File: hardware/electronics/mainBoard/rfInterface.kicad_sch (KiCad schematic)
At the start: 21 parts, among them J12 CONMHF1-SMD-T, J13 CONMHF1-SMD-T, J14 CONMHF1-SMD-T, J15 CONMHF1-SMD-T, U16 PMA2-162LNA+, U17 QCN-19D+

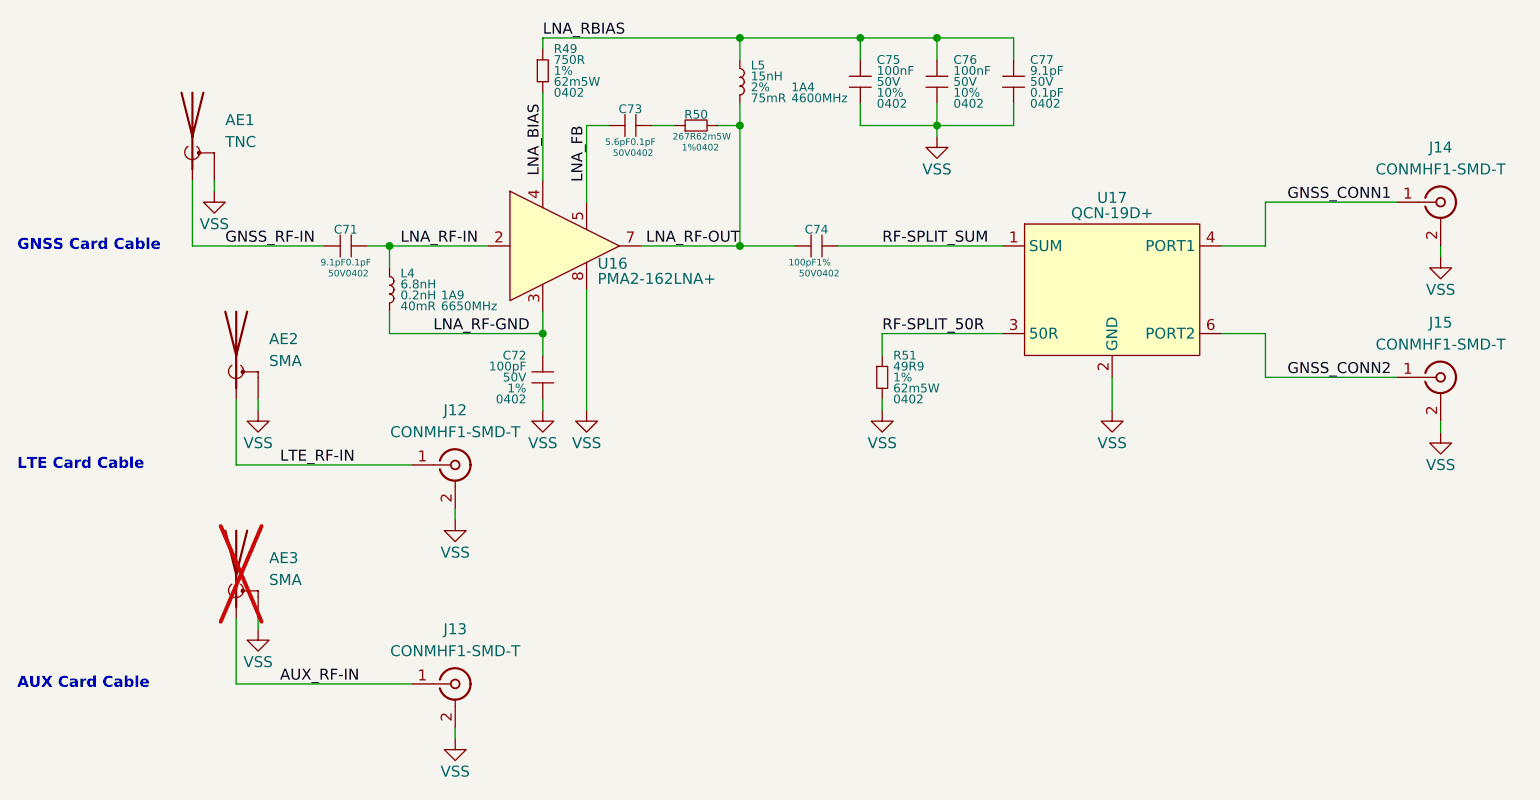
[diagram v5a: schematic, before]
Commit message: updated symbol refs
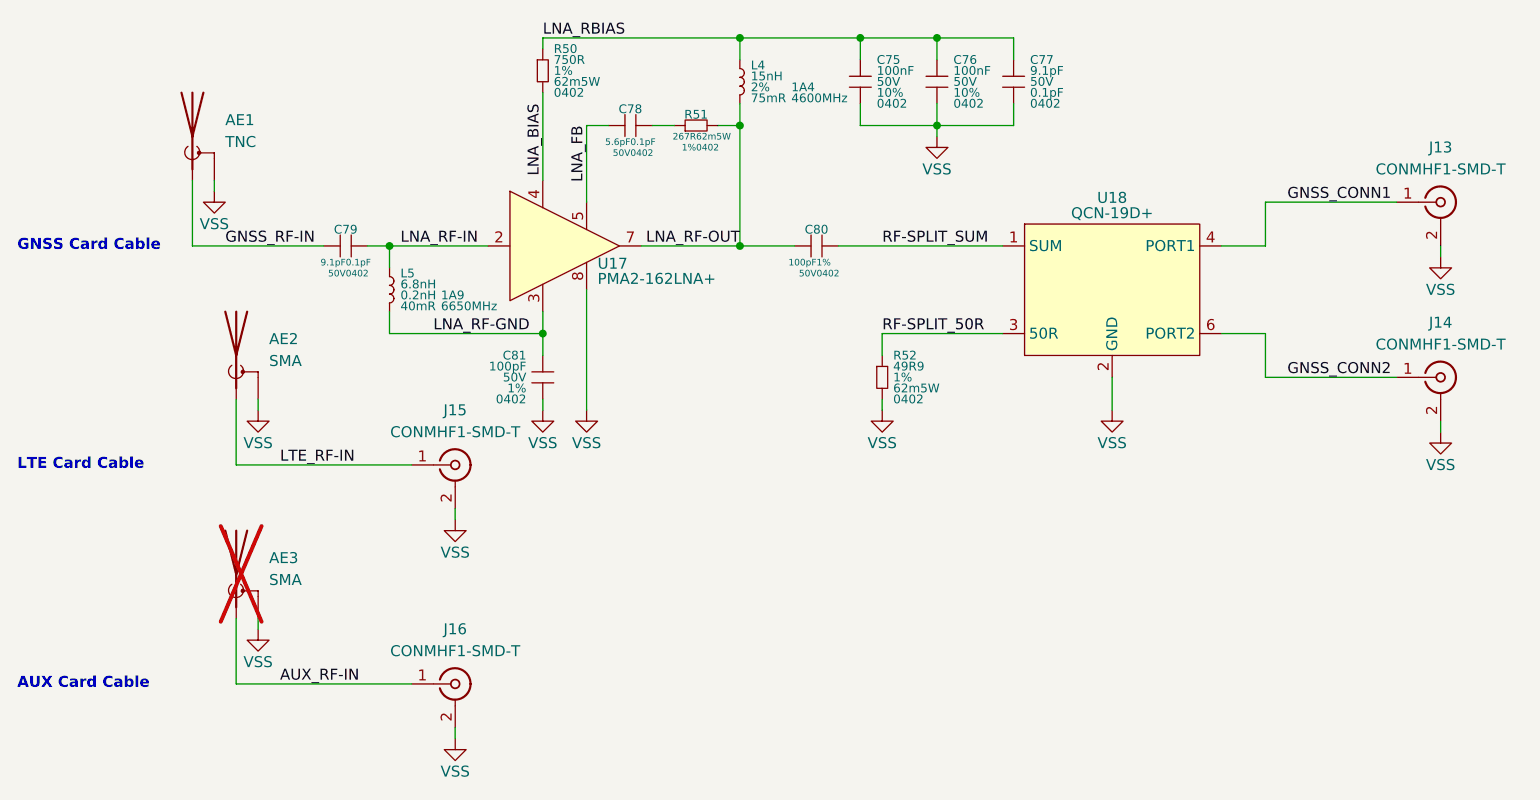
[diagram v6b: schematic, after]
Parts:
- renumbered C73 to C78, C71 to C79, C74 to C80, C72 to C81, J14 to J13, J15 to J14, J12 to J15, J13 to J16, L5 to L4, L4 to L5, R49 to R50, R50 to R51, R51 to R52, U16 to U17, U17 to U18
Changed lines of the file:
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@@
 		(dnp no)
 		(fields_autoplaced yes)
-		(property "Reference" "#PWR0172"
+		(property "Reference" "#PWR0184"
 			(at 114.3 133.35 0)
 			(effects
@@
 			(project "mainBoard"
 				(path "/be16e32f-2ccf-4272-9ec7-94d5fe7a55e0/9566ea48-a930-4cf1-864c-3e42d00ab717"
-					(reference "#PWR0172")
+					(reference "#PWR0184")
 					(unit 1)
 				)
@@
 		(dnp no)
 		(fields_autoplaced yes)
-		(property "Reference" "C74"
+		(property "Reference" "C80"
 			(at 156.21 74.295 0)
 			(do_not_autoplace yes)
@@
 			(project "mainBoard"
 				(path "/be16e32f-2ccf-4272-9ec7-94d5fe7a55e0/9566ea48-a930-4cf1-864c-3e42d00ab717"
-					(reference "C74")
+					(reference "C80")
 					(unit 1)
 				)
@@
 		(dnp no)
 		(fields_autoplaced yes)
-		(property "Reference" "R50"
+		(property "Reference" "R51"
 			(at 142.24 60.96 0)
 			(do_not_autoplace yes)
@@
 			(project ""
 				(path "/be16e32f-2ccf-4272-9ec7-94d5fe7a55e0/9566ea48-a930-4cf1-864c-3e42d00ab717"
-					(reference "R50")
+					(reference "R51")
 					(unit 1)
 				)
@@
 		(dnp no)
 		(fields_autoplaced yes)
-		(property "Reference" "#PWR0179"
+		(property "Reference" "#PWR0181"
 			(at 228.6 97.79 0)
 			(effects
@@
 			(project "mainBoard"
 				(path "/be16e32f-2ccf-4272-9ec7-94d5fe7a55e0/9566ea48-a930-4cf1-864c-3e42d00ab717"
-					(reference "#PWR0179")
+					(reference "#PWR0181")
 					(unit 1)
 				)
@@
 		(dnp no)
 		(fields_autoplaced yes)
-		(property "Reference" "#PWR0171"
+		(property "Reference" "#PWR0182"
 			(at 114.3 107.95 0)
 			(effects
@@
 			(project "mainBoard"
 				(path "/be16e32f-2ccf-4272-9ec7-94d5fe7a55e0/9566ea48-a930-4cf1-864c-3e42d00ab717"
-					(reference "#PWR0171")
+					(reference "#PWR0182")
 					(unit 1)
 				)
@@
 		(on_board yes)
 		(dnp no)
-		(property "Reference" "L4"
+		(property "Reference" "L5"
 			(at 107.95 79.375 0)
 			(do_not_autoplace yes)
@@
 			(project ""
 				(path "/be16e32f-2ccf-4272-9ec7-94d5fe7a55e0/9566ea48-a930-4cf1-864c-3e42d00ab717"
-					(reference "L4")
+					(reference "L5")
 					(unit 1)
 				)
@@
 		(dnp no)
 		(fields_autoplaced yes)
-		(property "Reference" "#PWR0170"
+		(property "Reference" "#PWR0183"
 			(at 91.44 120.65 0)
 			(effects
@@
 			(project "mainBoard"
 				(path "/be16e32f-2ccf-4272-9ec7-94d5fe7a55e0/9566ea48-a930-4cf1-864c-3e42d00ab717"
-					(reference "#PWR0170")
+					(reference "#PWR0183")
 					(unit 1)
 				)
@@
 		(on_board yes)
 		(dnp no)
-		(property "Reference" "J13"
+		(property "Reference" "J16"
 			(at 114.3 120.65 0)
 			(effects
@@
 			(project "mainBoard"
 				(path "/be16e32f-2ccf-4272-9ec7-94d5fe7a55e0/9566ea48-a930-4cf1-864c-3e42d00ab717"
-					(reference "J13")
+					(reference "J16")
 					(unit 1)
 				)
@@
 		(on_board yes)
 		(dnp no)
-		(property "Reference" "J14"
+		(property "Reference" "J13"
 			(at 228.6 64.77 0)
 			(effects
@@
 			(project ""
 				(path "/be16e32f-2ccf-4272-9ec7-94d5fe7a55e0/9566ea48-a930-4cf1-864c-3e42d00ab717"
-					(reference "J14")
+					(reference "J13")
 					(unit 1)
 				)
@@
 		(dnp no)
 		(fields_autoplaced yes)
-		(property "Reference" "#PWR0169"
+		(property "Reference" "#PWR0176"
 			(at 91.44 95.25 0)
 			(effects
@@
 			(project "mainBoard"
 				(path "/be16e32f-2ccf-4272-9ec7-94d5fe7a55e0/9566ea48-a930-4cf1-864c-3e42d00ab717"
-					(reference "#PWR0169")
+					(reference "#PWR0176")
 					(unit 1)
 				)
@@
 		(dnp no)
 		(fields_autoplaced yes)
-		(property "Reference" "R49"
+		(property "Reference" "R50"
 			(at 125.73 53.34 0)
 			(do_not_autoplace yes)
@@
 			(project ""
 				(path "/be16e32f-2ccf-4272-9ec7-94d5fe7a55e0/9566ea48-a930-4cf1-864c-3e42d00ab717"
-					(reference "R49")
+					(reference "R50")
 					(unit 1)
 				)
@@
 		(dnp no)
 		(fields_autoplaced yes)
-		(property "Reference" "#PWR0168"
+		(property "Reference" "#PWR0174"
 			(at 86.36 69.85 0)
 			(effects
@@
 			(project "mainBoard"
 				(path "/be16e32f-2ccf-4272-9ec7-94d5fe7a55e0/9566ea48-a930-4cf1-864c-3e42d00ab717"
-					(reference "#PWR0168")
+					(reference "#PWR0174")
 					(unit 1)
 				)
@@
 		(on_board yes)
 		(dnp no)
-		(property "Reference" "J15"
+		(property "Reference" "J14"
 			(at 228.6 85.09 0)
 			(effects
@@
 			(project "mainBoard"
 				(path "/be16e32f-2ccf-4272-9ec7-94d5fe7a55e0/9566ea48-a930-4cf1-864c-3e42d00ab717"
-					(reference "J15")
+					(reference "J14")
 					(unit 1)
 				)
@@
 		(on_board yes)
 		(dnp no)
-		(property "Reference" "L5"
+		(property "Reference" "L4"
 			(at 148.59 55.245 0)
 			(do_not_autoplace yes)
@@
 			(project "mainBoard"
 				(path "/be16e32f-2ccf-4272-9ec7-94d5fe7a55e0/9566ea48-a930-4cf1-864c-3e42d00ab717"
-					(reference "L5")
+					(reference "L4")
 					(unit 1)
 				)
@@
 		(dnp no)
 		(fields_autoplaced yes)
-		(property "Reference" "#PWR0175"
+		(property "Reference" "#PWR0179"
 			(at 163.83 95.25 0)
 			(effects
@@
 			(project "mainBoard"
 				(path "/be16e32f-2ccf-4272-9ec7-94d5fe7a55e0/9566ea48-a930-4cf1-864c-3e42d00ab717"
-					(reference "#PWR0175")
+					(reference "#PWR0179")
 					(unit 1)
 				)
@@
 		(dnp no)
 		(fields_autoplaced yes)
-		(property "Reference" "R51"
+		(property "Reference" "R52"
 			(at 165.1 88.9 0)
 			(do_not_autoplace yes)
@@
 			(project "mainBoard"
 				(path "/be16e32f-2ccf-4272-9ec7-94d5fe7a55e0/9566ea48-a930-4cf1-864c-3e42d00ab717"
-					(reference "R51")
+					(reference "R52")
 					(unit 1)
 				)
@@
 		(dnp no)
 		(fields_autoplaced yes)
-		(property "Reference" "#PWR0178"
+		(property "Reference" "#PWR0175"
 			(at 228.6 77.47 0)
 			(effects
@@
 			(project "mainBoard"
 				(path "/be16e32f-2ccf-4272-9ec7-94d5fe7a55e0/9566ea48-a930-4cf1-864c-3e42d00ab717"
-					(reference "#PWR0178")
+					(reference "#PWR0175")
 					(unit 1)
 				)
@@
 		(dnp no)
 		(fields_autoplaced yes)
-		(property "Reference" "#PWR0176"
+		(property "Reference" "#PWR0173"
 			(at 170.18 63.5 0)
 			(effects
@@
 			(project "mainBoard"
 				(path "/be16e32f-2ccf-4272-9ec7-94d5fe7a55e0/9566ea48-a930-4cf1-864c-3e42d00ab717"
-					(reference "#PWR0176")
+					(reference "#PWR0173")
 					(unit 1)
 				)
@@
 		(dnp no)
 		(fields_autoplaced yes)
-		(property "Reference" "C73"
+		(property "Reference" "C78"
 			(at 134.62 60.325 0)
 			(do_not_autoplace yes)
@@
 			(project "mainBoard"
 				(path "/be16e32f-2ccf-4272-9ec7-94d5fe7a55e0/9566ea48-a930-4cf1-864c-3e42d00ab717"
-					(reference "C73")
+					(reference "C78")
 					(unit 1)
 				)
@@
 		(dnp no)
 		(fields_autoplaced yes)
-		(property "Reference" "#PWR0173"
+		(property "Reference" "#PWR0177"
 			(at 124.46 95.25 0)
 			(effects
@@
 			(project "mainBoard"
 				(path "/be16e32f-2ccf-4272-9ec7-94d5fe7a55e0/9566ea48-a930-4cf1-864c-3e42d00ab717"
-					(reference "#PWR0173")
+					(reference "#PWR0177")
 					(unit 1)
 				)
@@
 		(dnp no)
 		(fields_autoplaced yes)
-		(property "Reference" "#PWR0177"
+		(property "Reference" "#PWR0180"
 			(at 190.5 95.25 0)
 			(effects
@@
 			(project "mainBoard"
 				(path "/be16e32f-2ccf-4272-9ec7-94d5fe7a55e0/9566ea48-a930-4cf1-864c-3e42d00ab717"
-					(reference "#PWR0177")
+					(reference "#PWR0180")
 					(unit 1)
 				)
@@
 		(dnp no)
 		(fields_autoplaced yes)
-		(property "Reference" "U16"
+		(property "Reference" "U17"
 			(at 130.81 78.994 0)
 			(do_not_autoplace yes)
@@
 			(project ""
 				(path "/be16e32f-2ccf-4272-9ec7-94d5fe7a55e0/9566ea48-a930-4cf1-864c-3e42d00ab717"
-					(reference "U16")
+					(reference "U17")
 					(unit 1)
 				)
@@
 		(on_board yes)
 		(dnp no)
-		(property "Reference" "J12"
+		(property "Reference" "J15"
 			(at 114.3 95.25 0)
 			(effects
@@
 			(project "mainBoard"
 				(path "/be16e32f-2ccf-4272-9ec7-94d5fe7a55e0/9566ea48-a930-4cf1-864c-3e42d00ab717"
-					(reference "J12")
+					(reference "J15")
 					(unit 1)
 				)
@@
 		(dnp no)
 		(fields_autoplaced yes)
-		(property "Reference" "C71"
+		(property "Reference" "C79"
 			(at 101.6 74.295 0)
 			(do_not_autoplace yes)
@@
 			(project ""
 				(path "/be16e32f-2ccf-4272-9ec7-94d5fe7a55e0/9566ea48-a930-4cf1-864c-3e42d00ab717"
-					(reference "C71")
+					(reference "C79")
 					(unit 1)
 				)
@@
 		(dnp no)
 		(fields_autoplaced yes)
-		(property "Reference" "U17"
+		(property "Reference" "U18"
 			(at 190.5 70.612 0)
 			(do_not_autoplace yes)
@@
 			(project ""
 				(path "/be16e32f-2ccf-4272-9ec7-94d5fe7a55e0/9566ea48-a930-4cf1-864c-3e42d00ab717"
-					(reference "U17")
+					(reference "U18")
 					(unit 1)
 				)
@@
 		(dnp no)
 		(fields_autoplaced yes)
-		(property "Reference" "#PWR0174"
+		(property "Reference" "#PWR0178"
 			(at 129.54 95.25 0)
 			(effects
@@
 			(project "mainBoard"
 				(path "/be16e32f-2ccf-4272-9ec7-94d5fe7a55e0/9566ea48-a930-4cf1-864c-3e42d00ab717"
-					(reference "#PWR0174")
+					(reference "#PWR0178")
 					(unit 1)
 				)
@@
 		(on_board yes)
 		(dnp no)
-		(property "Reference" "C72"
+		(property "Reference" "C81"
 			(at 122.555 88.9 0)
 			(do_not_autoplace yes)
@@
 			(project ""
 				(path "/be16e32f-2ccf-4272-9ec7-94d5fe7a55e0/9566ea48-a930-4cf1-864c-3e42d00ab717"
-					(reference "C72")
+					(reference "C81")
 					(unit 1)
 				)

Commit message: assigned FPs
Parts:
- AE1: footprint (none) -> lib_connectors:RFPC-TNC01-FN
- AE2, AE3: footprint (none) -> lib_connectors:RFPC-SMA14-FN
- J13, J14, J15, J16: footprint (none) -> lib_connectors:CONMHF1
- L4, L5: footprint (none) -> lib_passives:L_0603
- U17: footprint (none) -> lib_ICs:TFDFN200X200X100-8
- U18: footprint (none) -> lib_ICs:SON99P320X160X89-6
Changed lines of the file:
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@@
 			)
 		)
-		(property "Footprint" ""
+		(property "Footprint" "lib_passives:L_0603"
 			(at 106.68 80.01 90)
 			(effects
@@
 			)
 		)
-		(property "Footprint" ""
+		(property "Footprint" "lib_connectors:RFPC-SMA14-FN"
 			(at 88.9 86.36 0)
 			(effects
@@
 			)
 		)
-		(property "Footprint" ""
+		(property "Footprint" "lib_connectors:RFPC-SMA14-FN"
 			(at 88.9 111.76 0)
 			(effects
@@
 			)
 		)
-		(property "Footprint" ""
+		(property "Footprint" "lib_connectors:RFPC-TNC01-FN"
 			(at 83.82 60.96 0)
 			(effects
@@
 			)
 		)
-		(property "Footprint" ""
+		(property "Footprint" "lib_connectors:CONMHF1"
 			(at 114.3 127 0)
 			(effects
@@
 			)
 		)
-		(property "Footprint" ""
+		(property "Footprint" "lib_connectors:CONMHF1"
 			(at 228.6 71.12 0)
 			(effects
@@
 			)
 		)
-		(property "Footprint" ""
+		(property "Footprint" "lib_connectors:CONMHF1"
 			(at 228.6 91.44 0)
 			(effects
@@
 			)
 		)
-		(property "Footprint" ""
+		(property "Footprint" "lib_passives:L_0603"
 			(at 147.32 55.88 90)
 			(effects
@@
 			)
 		)
-		(property "Footprint" ""
+		(property "Footprint" "lib_ICs:TFDFN200X200X100-8"
 			(at 127 74.93 0)
 			(effects
@@
 			)
 		)
-		(property "Footprint" ""
+		(property "Footprint" "lib_connectors:CONMHF1"
 			(at 114.3 101.6 0)
 			(effects
@@
 			)
 		)
-		(property "Footprint" ""
+		(property "Footprint" "lib_ICs:SON99P320X160X89-6"
 			(at 190.5 81.28 0)
 			(effects

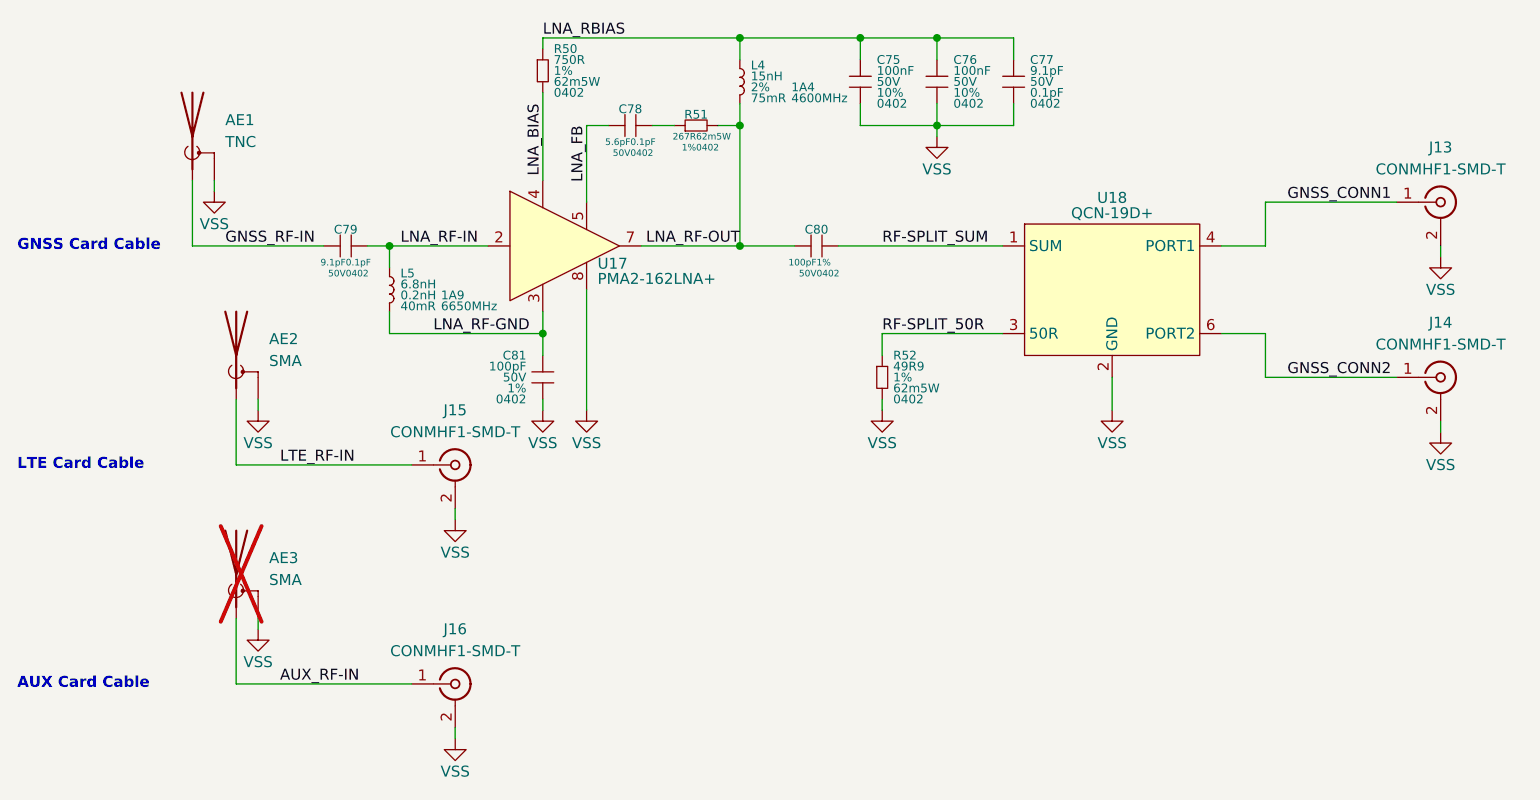
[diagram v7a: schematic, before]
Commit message: assigned footprints
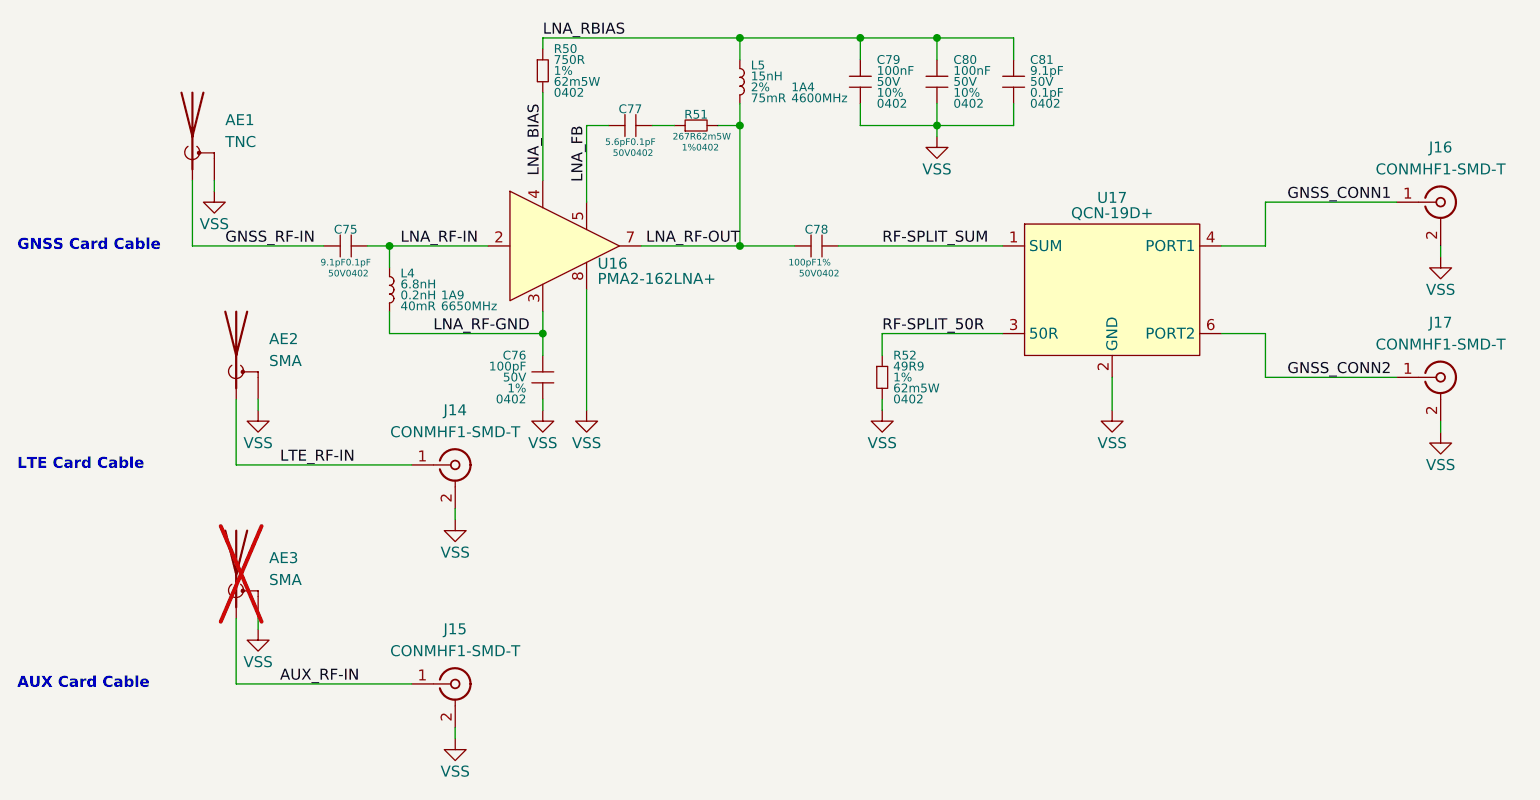
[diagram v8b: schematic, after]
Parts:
- C75: renamed from C79; footprint (none) -> lib_passives:GCM0402
- C76: renamed from C81; footprint (none) -> lib_passives:GCM0402
- C77: renamed from C78; footprint (none) -> lib_passives:GCM0402
- C78: renamed from C80; footprint (none) -> lib_passives:GCM0402
- C79: renamed from C75; footprint (none) -> lib_passives:GCM0402
- C80: renamed from C76; footprint (none) -> lib_passives:GCM0402
- C81: renamed from C77; footprint (none) -> lib_passives:GCM0402
- R50, R51, R52: footprint (none) -> lib_passives:CRCW0402
- renumbered J15 to J14, J16 to J15, J13 to J16, J14 to J17, L5 to L4, L4 to L5, U17 to U16, U18 to U17
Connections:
- net VSS: now also AE1.3 (Shield), AE1.4 (Shield), AE1.5 (Shield), AE2.3 (Shield), AE2.4 (Shield), AE2.5 (Shield), AE3.3 (Shield), AE3.4 (Shield), AE3.5 (Shield)
